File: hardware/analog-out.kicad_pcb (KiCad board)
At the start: 2 copper layers, 30 x 35 mm, 40 parts, among them P1 DEBUG, P2 CONN_5, P3 CON-SENSOR2, P4 BOOT, U1 XMC1XXX24, U2 MCP4725A0, U3 TLV272IS, U4 DRILL, U5 DRILL, U6 DRILL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

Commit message: Add fiducials
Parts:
- added Fiducial_Mark: VAL**, kicad-libraries:Fiducial_Mark, F.Cu at (146.1, 114.6)
- moved Fiducial_Mark 0.34 mm to (161.1, 113.6)
- moved Fiducial_Mark 0.20 mm to (144.1, 86.6)
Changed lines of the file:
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@@
     (tracks 316)
     (zones 0)
-    (modules 40)
+    (modules 41)
     (nets 43)
   )
@@
   )
   (setup
-    (last_trace_width 0.25)
+    (last_trace_width 0.14986)
     (user_trace_width 0.2)
     (user_trace_width 0.25)
@@
   )
   (module kicad-libraries:Fiducial_Mark (layer Vorderseite)
-    (at 144.25168 86.5759)
+    (at 144.05 86.575)
     (path Fiducial_Mark)
     (attr smd)
@@
   )
   (module kicad-libraries:Fiducial_Mark (layer Vorderseite)
-    (at 161.2 113.275)
+    (at 161.05 113.575)
     (path Fiducial_Mark)
     (attr smd)
@@
       (xy 1.301301 2.715081) (xy 1.302426 2.714986)) (layer B.SilkS) (width 0.01))
   )
+  (module kicad-libraries:Fiducial_Mark (layer Vorderseite)
+    (at 146.05 114.575)
+    (attr smd)
+    (fp_text reference Fiducial_Mark (at 0 0) (layer F.SilkS) hide
+      (effects (font (size 0.127 0.127) (thickness 0.03302)))
+    )
+    (fp_text value VAL** (at 0 -0.29972) (layer F.SilkS) hide
+      (effects (font (size 0.127 0.127) (thickness 0.03302)))
+    )
+    (fp_circle (center 0 0) (end 1.15062 0) (layer Dwgs.User) (width 0.01016))
+    (pad 1 smd circle (at 0 0) (size 1.00076 1.00076) (layers Vorderseite F.Paste F.Mask)
+      (clearance 0.65024))
+  )
   (gr_text Status (at 165.75 89.735) (layer F.SilkS)

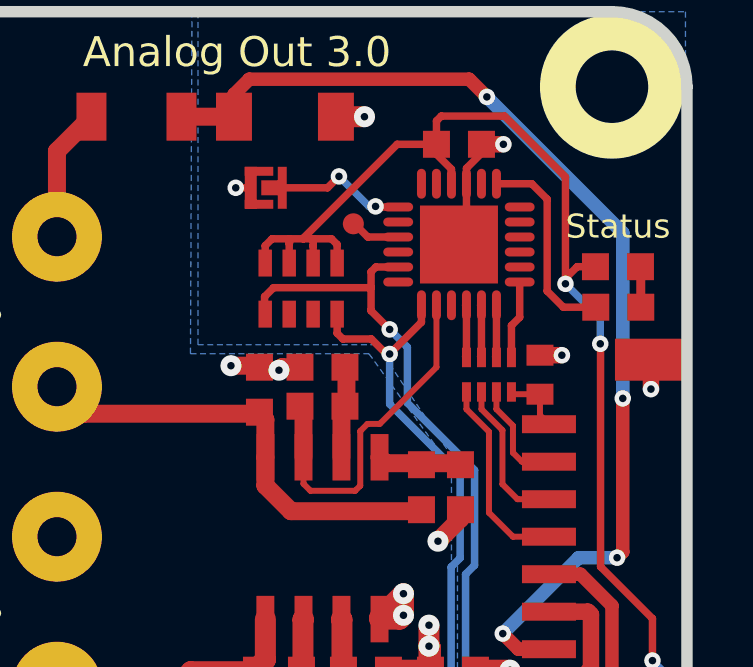
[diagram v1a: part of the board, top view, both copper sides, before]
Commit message: fix VIN routing, change LED pin
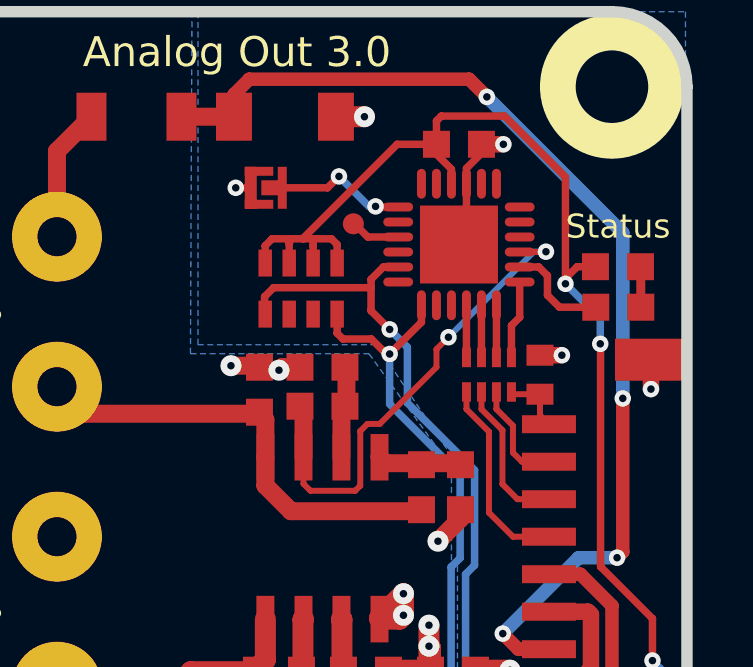
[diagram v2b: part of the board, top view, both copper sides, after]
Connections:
- RP2 pad 6: Net-(RP2-Pad6) -> (no net)
- RP2 pad 7: Net-(RP2-Pad7) -> (no net)
- U1 pad 11: Net-(U1-Pad11) -> (no net)
- U1 pad 12: Net-(U1-Pad12) -> (no net)
- U1 pad 14: Net-(U1-Pad14) -> (no net)
- U1 pad 16: Net-(U1-Pad16) -> (no net)
- U1 pad 18: Net-(U1-Pad18) -> (no net)
- U1 pad 2: Net-(U1-Pad2) -> Net-(R11-Pad1)
- U1 pad 20: VIN -> (no net)
- U1 pad 21: Net-(U1-Pad21) -> (no net)
- U1 pad 3: Net-(U1-Pad3) -> VIN
- U1 pad 4: Net-(U1-Pad4) -> (no net)
- U1 pad 5: Net-(U1-Pad5) -> (no net)
- U1 pad 6: Net-(U1-Pad6) -> (no net)
- U1 pad 7: Net-(R11-Pad1) -> (no net)
- U1 pad 8: Net-(U1-Pad8) -> (no net)
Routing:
- net VIN: track 12.0 -> 16.4 mm, vias 0 -> 2
- net Net-(R11-Pad1): track 6.81 -> 3.47 mm
